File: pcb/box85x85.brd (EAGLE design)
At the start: 74 x 74 mm, 28 parts, among them K1 ZF112, K2 ZF112, K3 ZF112, U1 LM1117-3.3, X1 MKDSN1,5/2-5,08, X2 MKDSN1,5/2-5,08, X3 MKDSN1,5/2-5,08, X4 MKDSN1,5/2-5,08

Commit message: ...
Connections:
- net N$12: now also IC2.11; no longer IC2.10
- net N$14: now also IC2.10; no longer IC2.13
- net N$5: now also IC2.13; no longer IC2.12
- net N$6: now also IC2.12; no longer IC2.11
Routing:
- net N$14: track 20.1 -> 15.8 mm
- net N$5: track 44.9 -> 43.2 mm
- net N$6: track 22.3 -> 20.6 mm
- net N$12: track 12.6 -> 13.1 mm
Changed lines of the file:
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@@
 </signal>
 <signal name="N$5">
-<contactref element="IC2" pad="12"/>
 <contactref element="K1" pad="2"/>
-<wire x1="38.9266" y1="55.635" x2="36.635" y2="55.635" width="0.4064" layer="1"/>
-<wire x1="36.635" y1="55.635" x2="36" y2="55" width="0.4064" layer="1"/>
-<wire x1="36" y1="55" x2="36" y2="46" width="0.4064" layer="1"/>
+<wire x1="36" y1="53" x2="36" y2="46" width="0.4064" layer="1"/>
 <wire x1="36" y1="46" x2="42" y2="40" width="0.4064" layer="1"/>
 <wire x1="42" y1="40" x2="42" y2="34" width="0.4064" layer="1"/>
@@
 <wire x1="29" y1="26" x2="27.1016" y2="26" width="0.4064" layer="1"/>
 <wire x1="27.1016" y1="26" x2="27.096" y2="25.9944" width="0.4064" layer="1"/>
+<contactref element="IC2" pad="13"/>
+<wire x1="38.9266" y1="54.365" x2="37.365" y2="54.365" width="0.4064" layer="1"/>
+<wire x1="37.365" y1="54.365" x2="36" y2="53" width="0.4064" layer="1"/>
 </signal>
 <signal name="N$6">
-<contactref element="IC2" pad="11"/>
 <contactref element="K2" pad="2"/>
-<wire x1="38.9266" y1="56.905" x2="35.905" y2="56.905" width="0.4064" layer="1"/>
-<wire x1="35.905" y1="56.905" x2="35" y2="56" width="0.4064" layer="1"/>
-<wire x1="35" y1="56" x2="35" y2="48" width="0.4064" layer="1"/>
+<wire x1="36.635" y1="55.635" x2="35" y2="54" width="0.4064" layer="1"/>
+<wire x1="35" y1="54" x2="35" y2="48" width="0.4064" layer="1"/>
 <wire x1="35" y1="48" x2="30" y2="43" width="0.4064" layer="1"/>
 <wire x1="30" y1="43" x2="27.1016" y2="43" width="0.4064" layer="1"/>
 <wire x1="27.1016" y1="43" x2="27.096" y2="42.9944" width="0.4064" layer="1"/>
+<contactref element="IC2" pad="12"/>
+<wire x1="38.9266" y1="55.635" x2="36.635" y2="55.635" width="0.4064" layer="1"/>
 </signal>
 <signal name="N$12">
-<contactref element="IC2" pad="10"/>
 <contactref element="K3" pad="2"/>
-<wire x1="38.9266" y1="58.175" x2="35.825" y2="58.175" width="0.4064" layer="1"/>
-<wire x1="35.825" y1="58.175" x2="34" y2="60" width="0.4064" layer="1"/>
-<wire x1="34" y1="60" x2="27.1016" y2="60" width="0.4064" layer="1"/>
+<wire x1="36.095" y1="56.905" x2="33" y2="60" width="0.4064" layer="1"/>
+<wire x1="33" y1="60" x2="27.1016" y2="60" width="0.4064" layer="1"/>
 <wire x1="27.1016" y1="60" x2="27.096" y2="59.9944" width="0.4064" layer="1"/>
+<contactref element="IC2" pad="11"/>
+<wire x1="38.9266" y1="56.905" x2="36.095" y2="56.905" width="0.4064" layer="1"/>
 </signal>
 <signal name="N$14">
-<contactref element="IC2" pad="13"/>
+<contactref element="IC2" pad="10"/>
 <contactref element="SG1" pad="-"/>
-<wire x1="38.9266" y1="54.365" x2="40.365" y2="54.365" width="0.4064" layer="1"/>
-<wire x1="40.365" y1="54.365" x2="42" y2="56" width="0.4064" layer="1"/>
-<wire x1="42" y1="56" x2="42" y2="65.2512" width="0.4064" layer="1"/>
-<wire x1="42" y1="65.2512" x2="37" y2="70.2512" width="0.4064" layer="1"/>
+<wire x1="38.9266" y1="58.175" x2="36.825" y2="58.175" width="0.4064" layer="1"/>
+<wire x1="35" y1="60" x2="35" y2="68.2512" width="0.4064" layer="1"/>
+<wire x1="35" y1="68.2512" x2="37" y2="70.2512" width="0.4064" layer="1"/>
+<wire x1="36.825" y1="58.175" x2="35" y2="60" width="0.4064" layer="1"/>
 </signal>
 </signals>

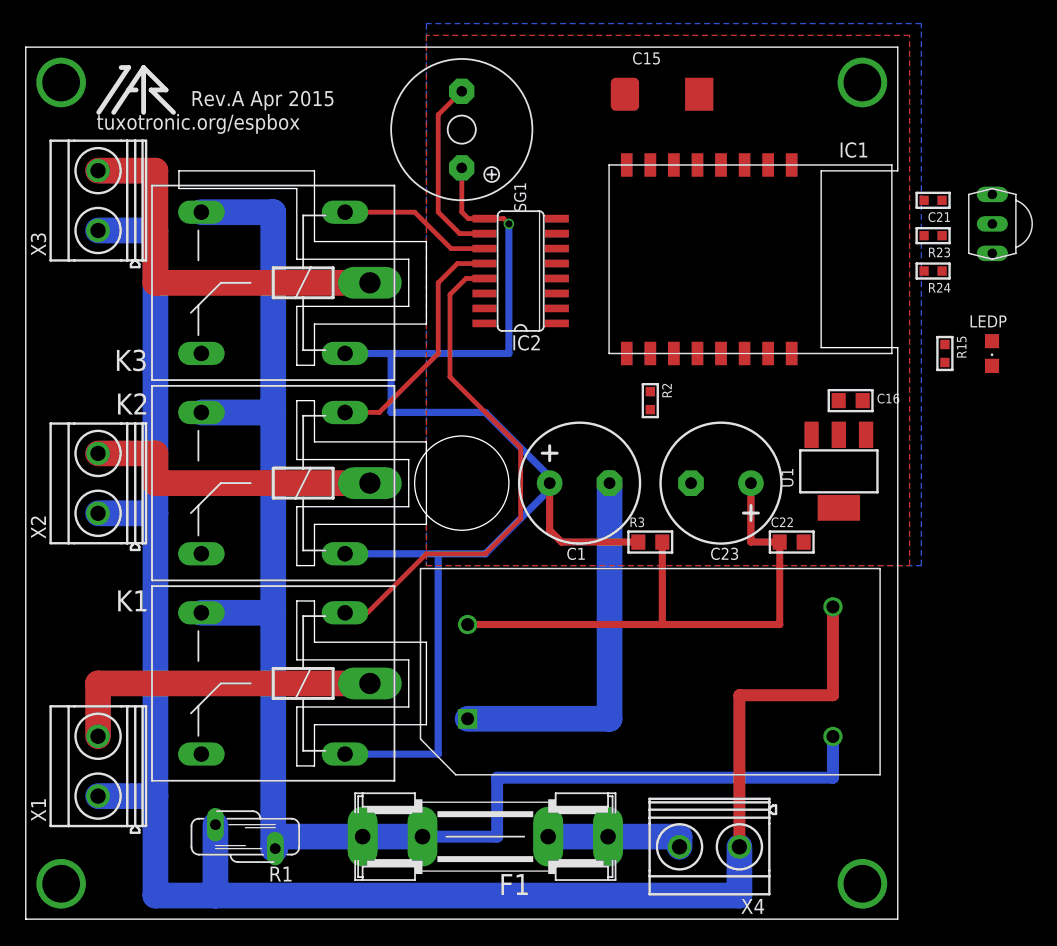
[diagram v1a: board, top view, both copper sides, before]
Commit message: pcb in progress.  connect relays
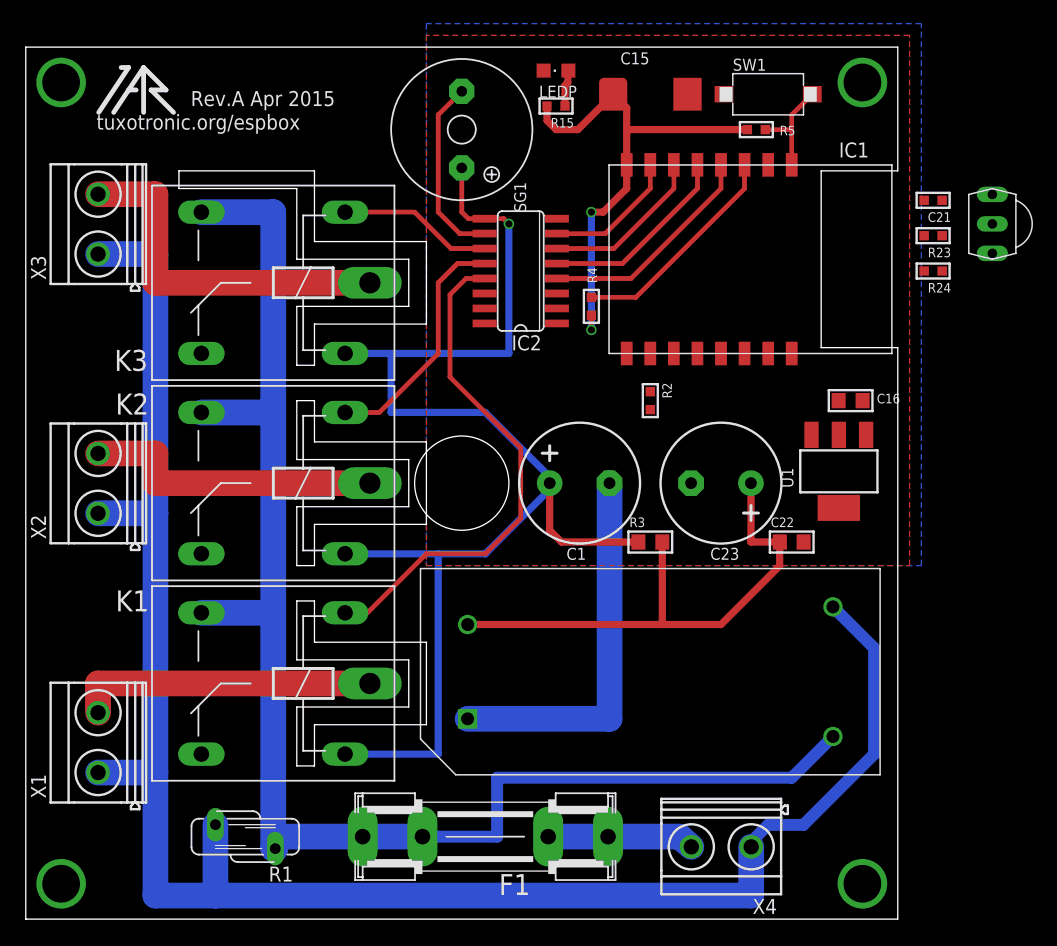
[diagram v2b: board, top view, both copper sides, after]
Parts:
- added R4: 10, rc-master-smd:R0603
- added R5: 10K, rc-master-smd:R0603
- added SW1: KSS-2EG4430, buttons:KSS-2EG4430
- moved LEDP 44.1 mm to (45.0, 72.0), turned to 90 degrees
- moved R15 39.1 mm to (45.0, 69.0), turned to 180 degrees
- moved X1 2.00 mm to (6.16, 15.0)
- moved X3 2.00 mm to (6.16, 59.0)
- moved C15 1.00 mm to (53.0, 70.0)
- moved X4 1.00 mm to (59.0, 6.16)
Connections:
- new net BUZ: IC1.7, IC2.7
- new net N$15: IC1.3, R4.2
- new net N$16: IC1.1, R5.2, SW1.2
- new net REL1: IC1.4, IC2.4
- new net REL2: IC1.5, IC2.5
- new net REL3: IC1.6, IC2.6
- net +3V3: now also R15.2, R4.1, R5.1
- net +5V: no longer R15.2
- net GND: now also IC2.1, IC2.2, IC2.3, SW1.1
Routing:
- net +3V3: track 0.00 -> 42.2 mm, vias 0 -> 2
- net REL1: track 0.00 -> 19.1 mm
- net N$15: track 0.00 -> 18.8 mm
- net REL2: track 0.00 -> 16.6 mm
- net REL3: track 0.00 -> 14.0 mm
- net BUZ: track 0.00 -> 11.5 mm
- net N$16: track 0.00 -> 8.96 mm
- net N$46: track 0.00 -> 3.12 mm
- net +5V: track 47.9 -> 45.0 mm
- net ACTIVE: track 129.3 -> 127.3 mm
- net N$4: track 32.6 -> 30.6 mm
- net N$2: track 27.6 -> 25.6 mm
- net NEITRAL: track 159.0 -> 157.6 mm

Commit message: PCB ready for LUT
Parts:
- added JP1: (no value), pinhead-fixdrills:2X05
- added LED1, LED2, LED3: (no value), led:LED3MM
- added R10, R9: 10K, rc-master-smd:R0805
- added R6, R7, R8: 470, rc-master-smd:R0805
- C1, C23: device rc-master:CE-050X100 -> rc-master:CE-035X080
- C21: device rc-master-smd:C0603 -> rc-master-smd:C0805
- LEDP: device led:CHIPLED_0805 -> led:LED3MM
- R15, R2, R23, R24, R4, R5: device rc-master-smd:R0603 -> rc-master-smd:R0805
- R3: value 100 -> 10
- moved U$1 66.0 mm to (11.0, 5.00)
- moved C16 30.5 mm to (47.0, 64.0), turned to 180 degrees
- moved IR1 25.1 mm to (70.0, 37.0)
- moved U1 24.1 mm to (53.0, 56.0), flipped to the bottom, turned to 270 degrees
- moved R24 23.1 mm to (65.5, 35.0)
- moved R23 22.2 mm to (65.5, 39.0)
- moved C21 21.0 mm to (68.0, 42.0)
- moved R4 19.2 mm to (60.0, 67.0), turned to 0 degrees
- moved R2 5.83 mm to (48.0, 47.0), turned to 90 degrees
- moved C1 3.00 mm to (47.0, 34.0)
- moved C23 3.00 mm to (59.0, 34.0)
- moved R15 2.24 mm to (46.0, 67.0), turned to 0 degrees
- moved R5 2.00 mm to (64.0, 67.0)
- moved ACDC1 1.00 mm to (53.0, 20.0)
- moved C15 1.00 mm to (53.0, 71.0)
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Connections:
- removed net N$13: C1.+, IC2.9, K1.1, K2.1, K3.1, R3.1, SG1.+
- new net +5V_FILTER: C1.+, IC2.9, K1.1, K2.1, K3.1, LED1.A, LED2.A, LED3.A, R3.1, SG1.+
- new net ADC: IC1.2, JP1.7
- new net GPIO0: IC1.12, JP1.5, R9.1
- new net GPIO15: IC1.10, JP1.4, R2.1
- new net GPIO2: IC1.11, JP1.6, R10.1
- new net GPIO5: IC1.13, JP1.8
- new net N$17: LED2.K, R7.1
- new net N$18: LED3.K, R8.1
- new net RXD: IC1.15, JP1.10
- new net TXD: IC1.16, JP1.9
- net +3V3: now also JP1.2, R10.2, R24.2, R9.2, U1.4
- net +5V: now also JP1.1; no longer R24.2
- net GND: now also JP1.3, LEDP.K; no longer LEDP.C
- net IR: now also IC1.14
- net N$11: now also LED1.K, R6.1; no longer IC1.10, R2.1
- net N$12: now also R8.2
- net N$5: now also R6.2
- net N$6: now also R7.2
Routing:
- net +5V_FILTER: track 0.00 -> 138.7 mm, vias 0 -> 1
- net N$13: track 111.3 -> 0.00 mm, vias 1 -> 0
- net +3V3: track 42.2 -> 93.6 mm
- net +5V: track 45.0 -> 87.4 mm, vias 0 -> 1
- net N$12: track 13.1 -> 49.4 mm
- net N$6: track 20.6 -> 54.2 mm
- net IR: track 0.00 -> 29.2 mm
- net N$5: track 43.2 -> 71.3 mm
- net ADC: track 0.00 -> 25.2 mm
- net GPIO0: track 0.00 -> 20.4 mm
- net N$15: track 18.8 -> 3.00 mm
- net GPIO2: track 0.00 -> 14.1 mm
- net GPIO15: track 0.00 -> 9.92 mm
- net GND: track 32.0 -> 22.3 mm, vias 0 -> 47
- net TXD: track 0.00 -> 9.27 mm
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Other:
- board text added: "+3V3"
- board text added: "+5V"
- board text added: "A"
- board text added: "ADC"
- board text added: "GND"
- board text added: "IO0"
- board text added: "IO15"
- board text added: "IO2"
- board text added: "IO5"
- board text added: "N"
- board text added: "RXD"
- board text added: "TXD"

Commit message: nice wires
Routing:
- net N$5: track 71.3 -> 66.3 mm
- net N$6: track 54.2 -> 51.2 mm
- net +5V_FILTER: track 138.7 -> 136.3 mm
- net +3V3: track 93.6 -> 91.9 mm
- net GPIO0: track 20.4 -> 19.2 mm
- net N$12: track 49.4 -> 48.2 mm
- net ADC: track 25.2 -> 24.3 mm
- net RXD: track 6.22 -> 5.34 mm
- net N$14: track 15.8 -> 15.0 mm
- net TXD: track 9.27 -> 8.57 mm
- net GPIO2: track 14.1 -> 13.5 mm
- net REL1: track 18.8 -> 18.2 mm
- net +5V: track 87.4 -> 86.8 mm

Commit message: ...
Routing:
- net NEITRAL: track 150.1 -> 148.1 mm
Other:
- board text added: "BOTTOM"
- board text added: "TOP"
